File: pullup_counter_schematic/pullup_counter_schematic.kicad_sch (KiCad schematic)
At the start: 67 parts, among them J1 USB_B_Micro, J2 6PinDebugPort, J3 Micro_SD_Card, Q1 MMBT3904, SW1 boot, SW2 rst, SW3 dataDump, SW4 start, U1 MT3608, U2 STM32G070RBT6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

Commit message: Changed proximity sens to SMD, added more USR btns
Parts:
- removed R13: 10K, Resistor_SMD:R_0805_2012Metric_Pad1.20x1.40mm_HandSolder, symbol Device:R
- removed U4: TCRT5000, TCRT5000:TCRT5000, symbol TCRT5000:TCRT5000
- added SW5: UsrBtn1, custom_buttons_switches:TSB008, symbol Switch:SW_Push
- added SW6: UsrBtn2, custom_buttons_switches:TSB008, symbol Switch:SW_Push
- added SW7: UsrBtn3, custom_buttons_switches:TSB008, symbol Switch:SW_Push
- added U4: ITR8307, OptoDevice:Everlight_ITR8307, symbol Sensor_Proximity:ITR8307
- SW3: value dataDump -> UsrBtn0
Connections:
- net GND: now also SW5.2, SW6.2, SW7.2, U4.4 (E)
- net PROX_OUT: now also U4.3 (C)
- net at R22.1: now also U4.2 (A)
- net at Q1.3 (C): now also U4.1 (K)
- net UsrBtn3: now reaches U2.51 (PD1)
- net UsrBtn3: now also SW7.1
- net UsrBtn2: now reaches U2.52 (PD2)
- net UsrBtn2: now also SW5.1
- net UsrBtn1: now reaches U2.53 (PD3)
- net UsrBtn1: now also SW6.1
- net dataDump renamed UsrBtn0
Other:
- moved on the sheet: Q1, R10, R12, R21, R23, SW1, SW3

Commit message: Minor fixes
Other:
- note added: "OLED Display"
- note added: "SD Card"
- note added: "Start button"
- note removed: "Display"
- moved on the sheet: BT1, BT2, BT3, C1, C10, C11, C12, C13, C14, C15, C17, C18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

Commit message: Deleted unnecessary files in schematic
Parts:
- R2: value R -> 16K
- R3: value R -> 3K6

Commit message: Fixed SPI Flash; Started work on proximity sensor
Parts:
- R21: value 1K2 -> 100R
- R22: value 220R -> 0R
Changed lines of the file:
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@@
       (effects (font (size 1.27 1.27)) (justify left))
     )
-    (property "Value" "220R" (at 59.817 70.358 0)
+    (property "Value" "0R" (at 59.817 70.358 0)
       (effects (font (size 1.27 1.27)) (justify left))
     )
@@
       (effects (font (size 1.27 1.27)) (justify left))
     )
-    (property "Value" "1K2" (at 52.197 83.058 0)
-      (effects (font (size 1.27 1.27)) (justify left))
-    )
+    (property "Value" "100R" (at 52.197 83.058 0)
+      (effects (font (size 1.27 1.27)) (justify left))
+    )

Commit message: some debugging/schematic fixing
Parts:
- R21: value 100R -> 470R
- R22: value 0R -> 100R
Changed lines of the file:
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@@
       (effects (font (size 1.27 1.27)) (justify left))
     )
-    (property "Value" "0R" (at 59.817 70.358 0)
+    (property "Value" "100R" (at 59.817 70.358 0)
       (effects (font (size 1.27 1.27)) (justify left))
     )
@@
       (effects (font (size 1.27 1.27)) (justify left))
     )
-    (property "Value" "100R" (at 52.197 83.058 0)
-      (effects (font (size 1.27 1.27)) (justify left))
-    )
+    (property "Value" "470R" (at 52.197 83.058 0)
+      (effects (font (size 1.27 1.27)) (justify left))
+    )

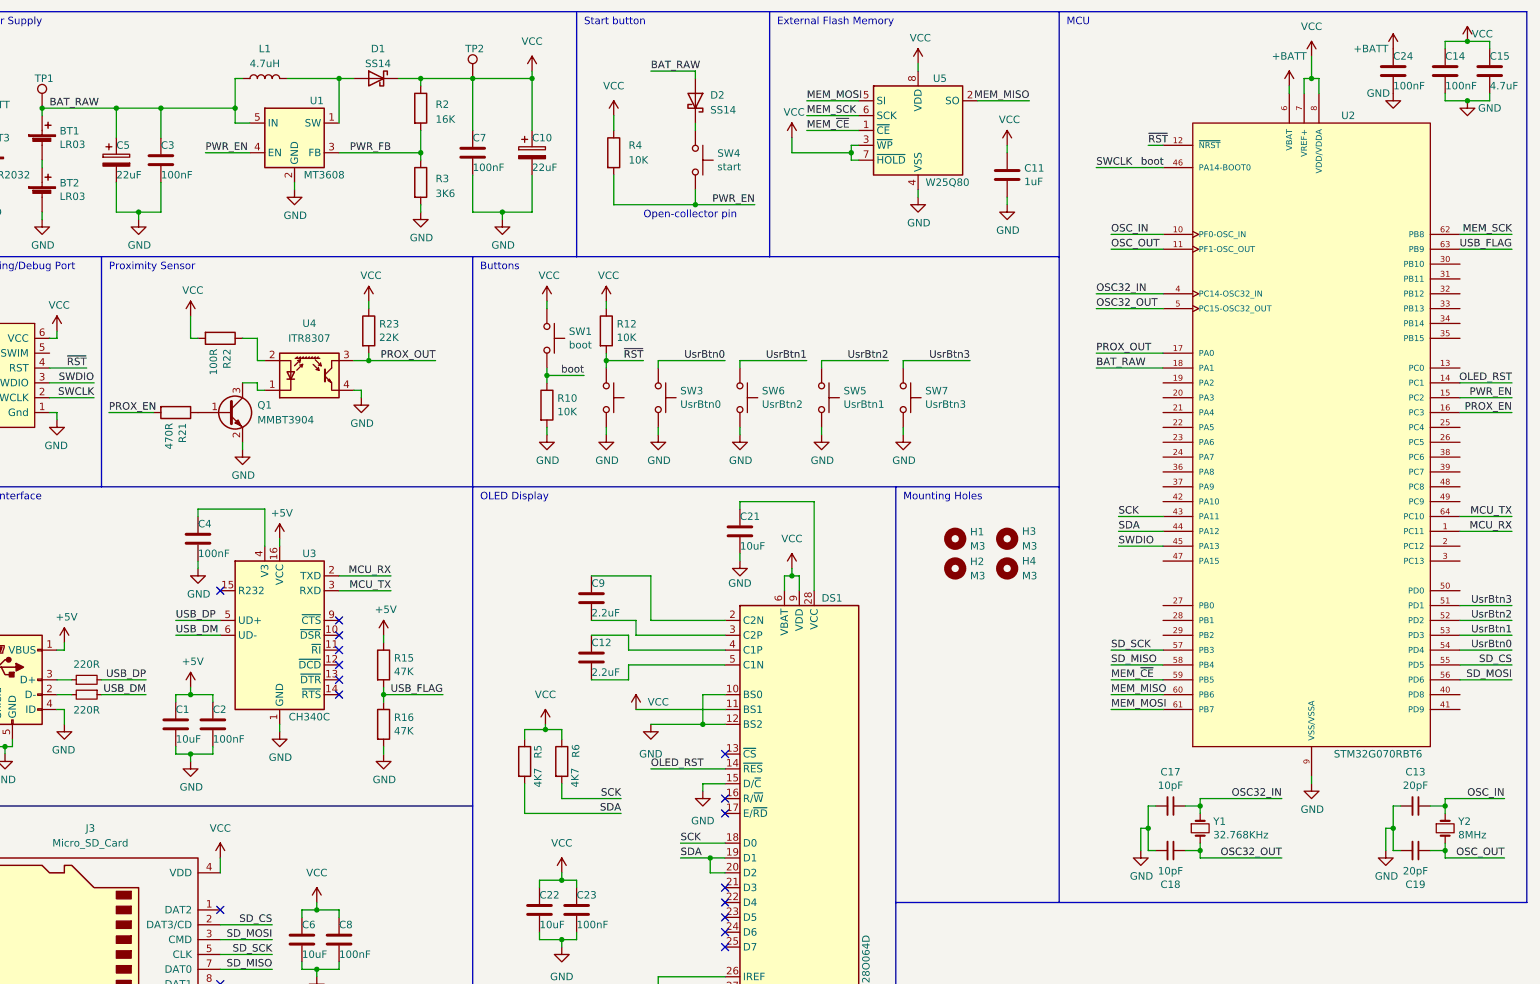
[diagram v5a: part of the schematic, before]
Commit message: cleared up kicads libs and footprints
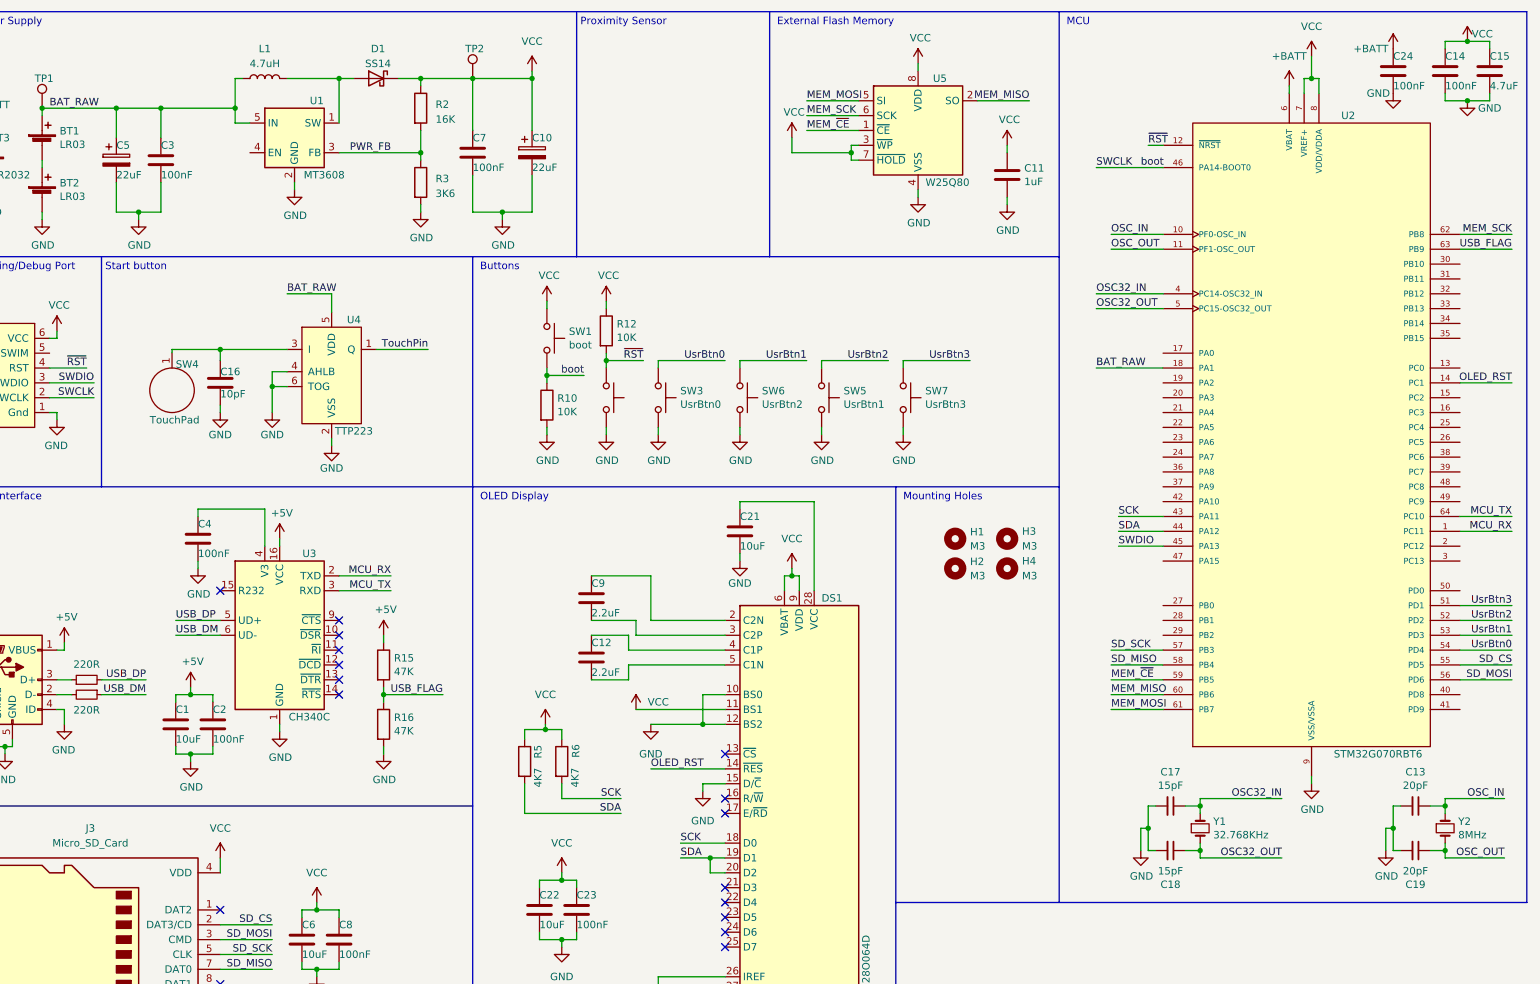
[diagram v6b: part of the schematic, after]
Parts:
- removed D2: SS14, Diode_SMD:D_SMA, symbol Device:D_Schottky
- removed Q1: MMBT3904, Package_TO_SOT_SMD:SOT-23, symbol Transistor_BJT:MMBT3904
- removed R21: 470R, Resistor_SMD:R_0805_2012Metric_Pad1.20x1.40mm_HandSolder, symbol Device:R
- removed R22: 100R, Resistor_SMD:R_0805_2012Metric_Pad1.20x1.40mm_HandSolder, symbol Device:R
- removed R23: 22K, Resistor_SMD:R_0805_2012Metric_Pad1.20x1.40mm_HandSolder, symbol Device:R
- removed R4: 10K, Resistor_SMD:R_0805_2012Metric_Pad1.20x1.40mm_HandSolder, symbol Device:R
- removed SW4: start, custom_buttons_switches:sw_push_12_x_12_mm, symbol Switch:SW_Push
- removed U4: ITR8307, OptoDevice:Everlight_ITR8307, symbol Sensor_Proximity:ITR8307
- added C16: 10pF, symbol Device:C
- added SW4: TouchPad, symbol TouchPad:TouchPad
- added U4: TTP223, Package_TO_SOT_SMD:TSOT-23-6_HandSoldering, symbol TTP:TTP223
- C17, C18: value 10pF -> 15pF
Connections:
- net BAT_RAW: now also U4.5 (VDD)
- net GND: now also C16.2, U4.2 (VSS), U4.4 (AHLB), U4.6 (TOG)
- net PROX_EN: no longer names the net of U2.16 (PC3)
- net PROX_OUT: no longer names the net of U2.17 (PA0)
- net PWR_EN: no longer names the net of U2.15 (PC2)
- net PWR_EN: no longer U1.4 (EN)
- new net: C16.1, SW4.1, U4.3 (I)
- new net TouchPin: U4.1 (Q)
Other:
- note removed: "Open-collector pin"
